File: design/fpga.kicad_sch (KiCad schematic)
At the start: 83 parts, among them J7 DEBUG_FPGA_GPIO, J8 DIGILENT_JTAG_HS2_01X06, SW1 RST, SW2 PROG, U13 XC7S15-FTGB196, U14 IS25LP064A-JKx

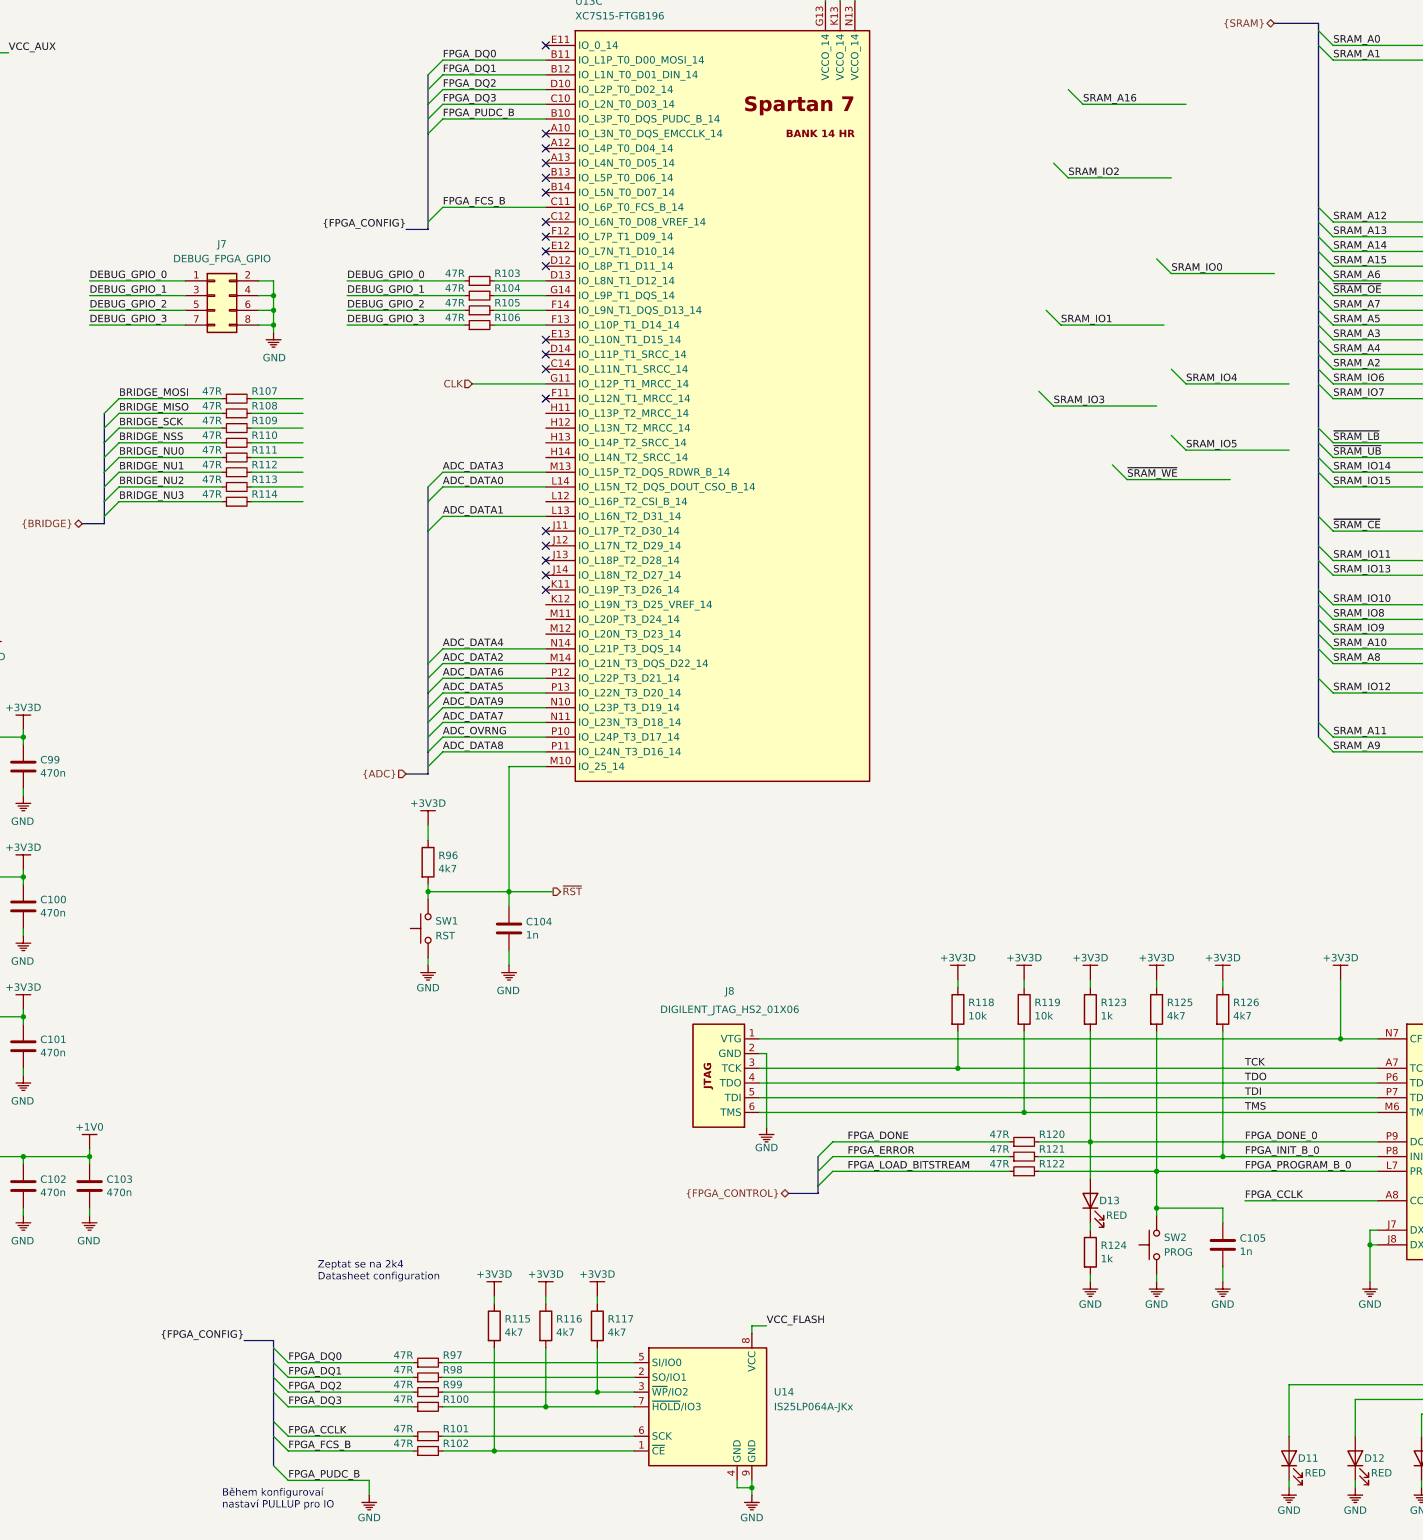
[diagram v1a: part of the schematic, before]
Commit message: Updated ADC layout
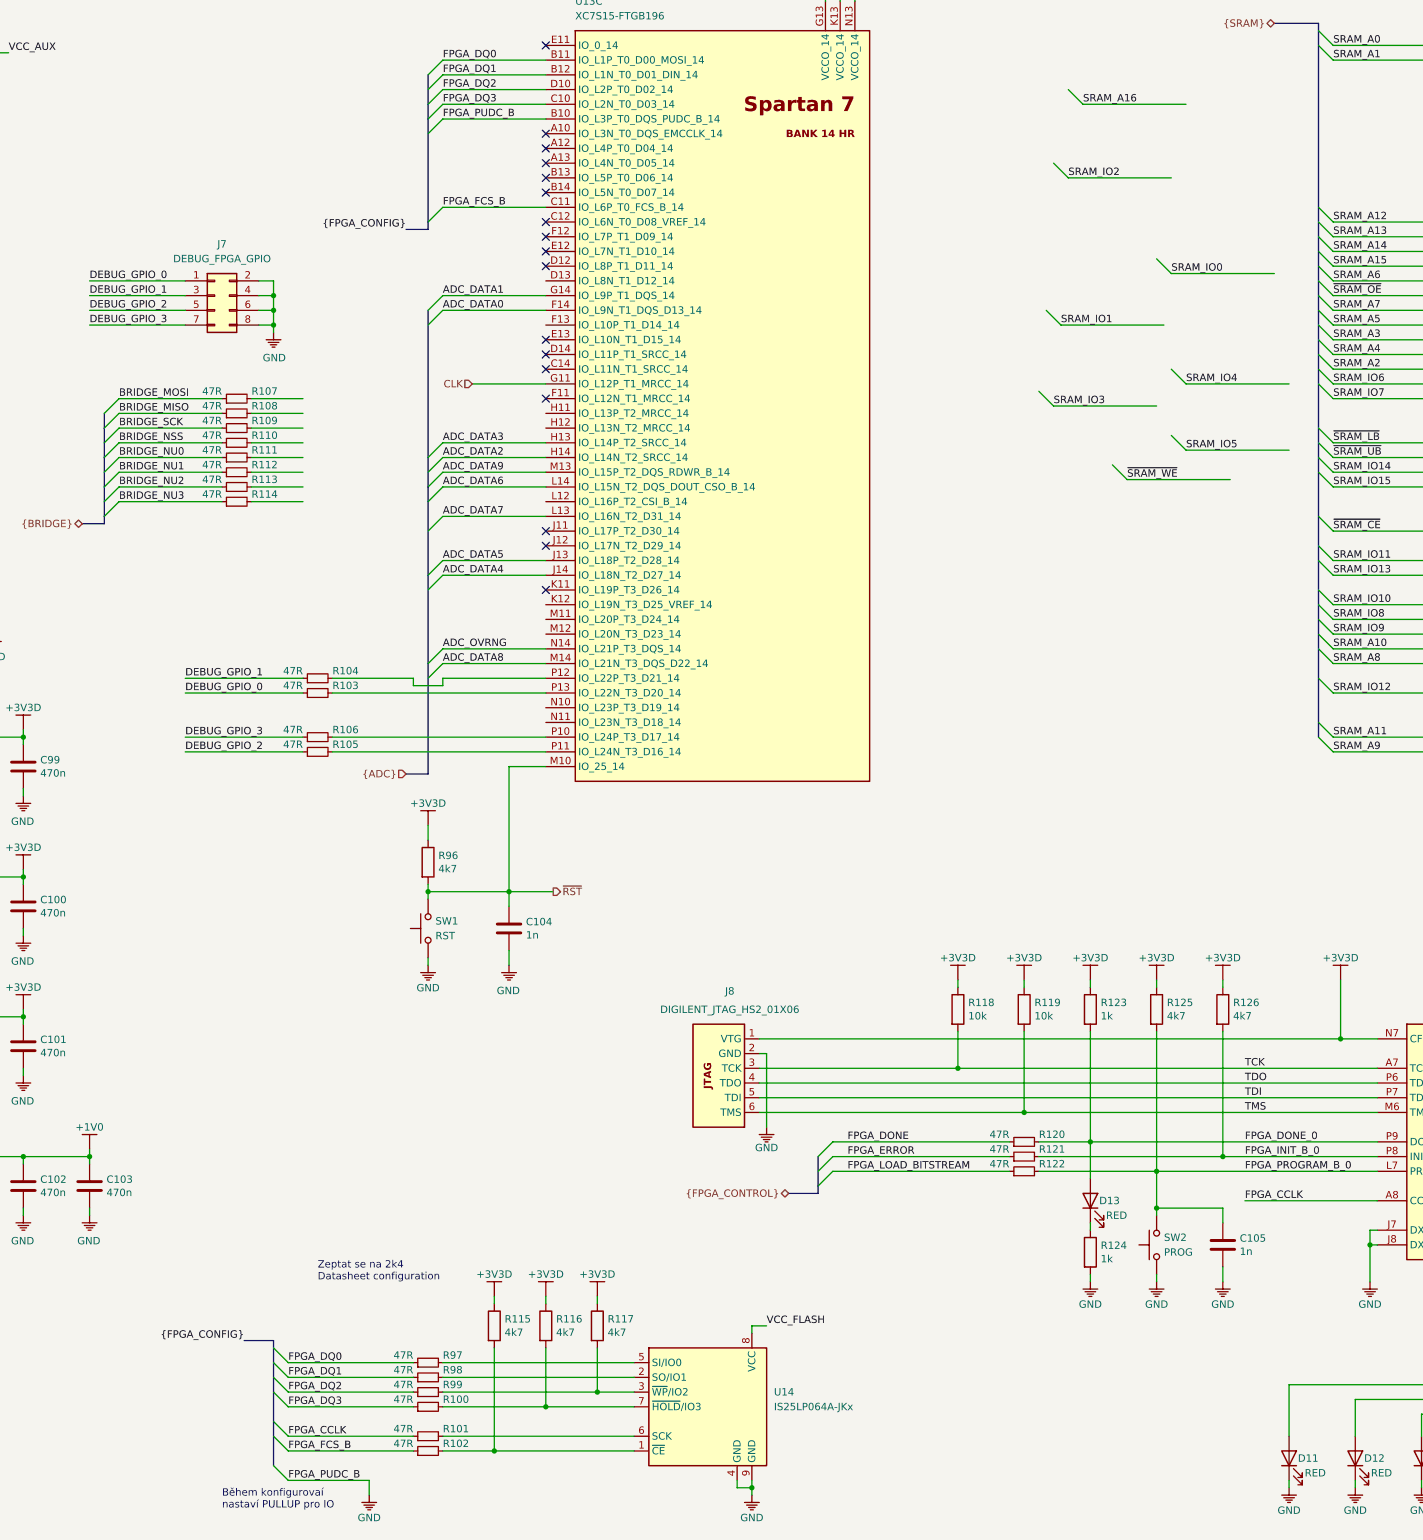
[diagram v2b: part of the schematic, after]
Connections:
- net ADC_DATA0: now also U13.F14 (IO_L9N_T1_DQS_D13_14); no longer U13.L14 (IO_L15N_T2_DQS_DOUT_CSO_B_14)
- net ADC_DATA1: now also U13.G14 (IO_L9P_T1_DQS_14); no longer U13.L13 (IO_L16N_T2_D31_14)
- net ADC_DATA2: now also U13.H14 (IO_L14N_T2_SRCC_14); no longer U13.M14 (IO_L21N_T3_DQS_D22_14)
- net ADC_DATA3: now also U13.H13 (IO_L14P_T2_SRCC_14); no longer U13.M13 (IO_L15P_T2_DQS_RDWR_B_14)
- net ADC_DATA4: now also U13.J14 (IO_L18N_T2_D27_14); no longer U13.N14 (IO_L21P_T3_DQS_14)
- net ADC_DATA5: now also U13.J13 (IO_L18P_T2_D28_14); no longer U13.P13 (IO_L22N_T3_D20_14)
- net ADC_DATA6: now also U13.L14 (IO_L15N_T2_DQS_DOUT_CSO_B_14); no longer U13.P12 (IO_L22P_T3_D21_14)
- net ADC_DATA7: now also U13.L13 (IO_L16N_T2_D31_14); no longer U13.N11 (IO_L23N_T3_D18_14)
- net ADC_DATA8: now also U13.M14 (IO_L21N_T3_DQS_D22_14); no longer U13.P11 (IO_L24N_T3_D16_14)
- net ADC_DATA9: now also U13.M13 (IO_L15P_T2_DQS_RDWR_B_14); no longer U13.N10 (IO_L23P_T3_D19_14)
- net ADC_OVRNG: now also U13.N14 (IO_L21P_T3_DQS_14); no longer U13.P10 (IO_L24P_T3_D17_14)
- net at R105.2: now also U13.P11 (IO_L24N_T3_D16_14); no longer U13.F14 (IO_L9N_T1_DQS_D13_14)
- net at R104.2: now also U13.P12 (IO_L22P_T3_D21_14); no longer U13.G14 (IO_L9P_T1_DQS_14)
- net at R103.2: now also U13.P13 (IO_L22N_T3_D20_14); no longer U13.D13 (IO_L8N_T1_D12_14)
- net at U13.F13 (IO_L10P_T1_D14_14): no longer R106.2
- new net: R106.2, U13.P10 (IO_L24P_T3_D17_14)
- no-connect marks 19 -> 17
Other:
- moved on the sheet: R103, R104, R105, R106

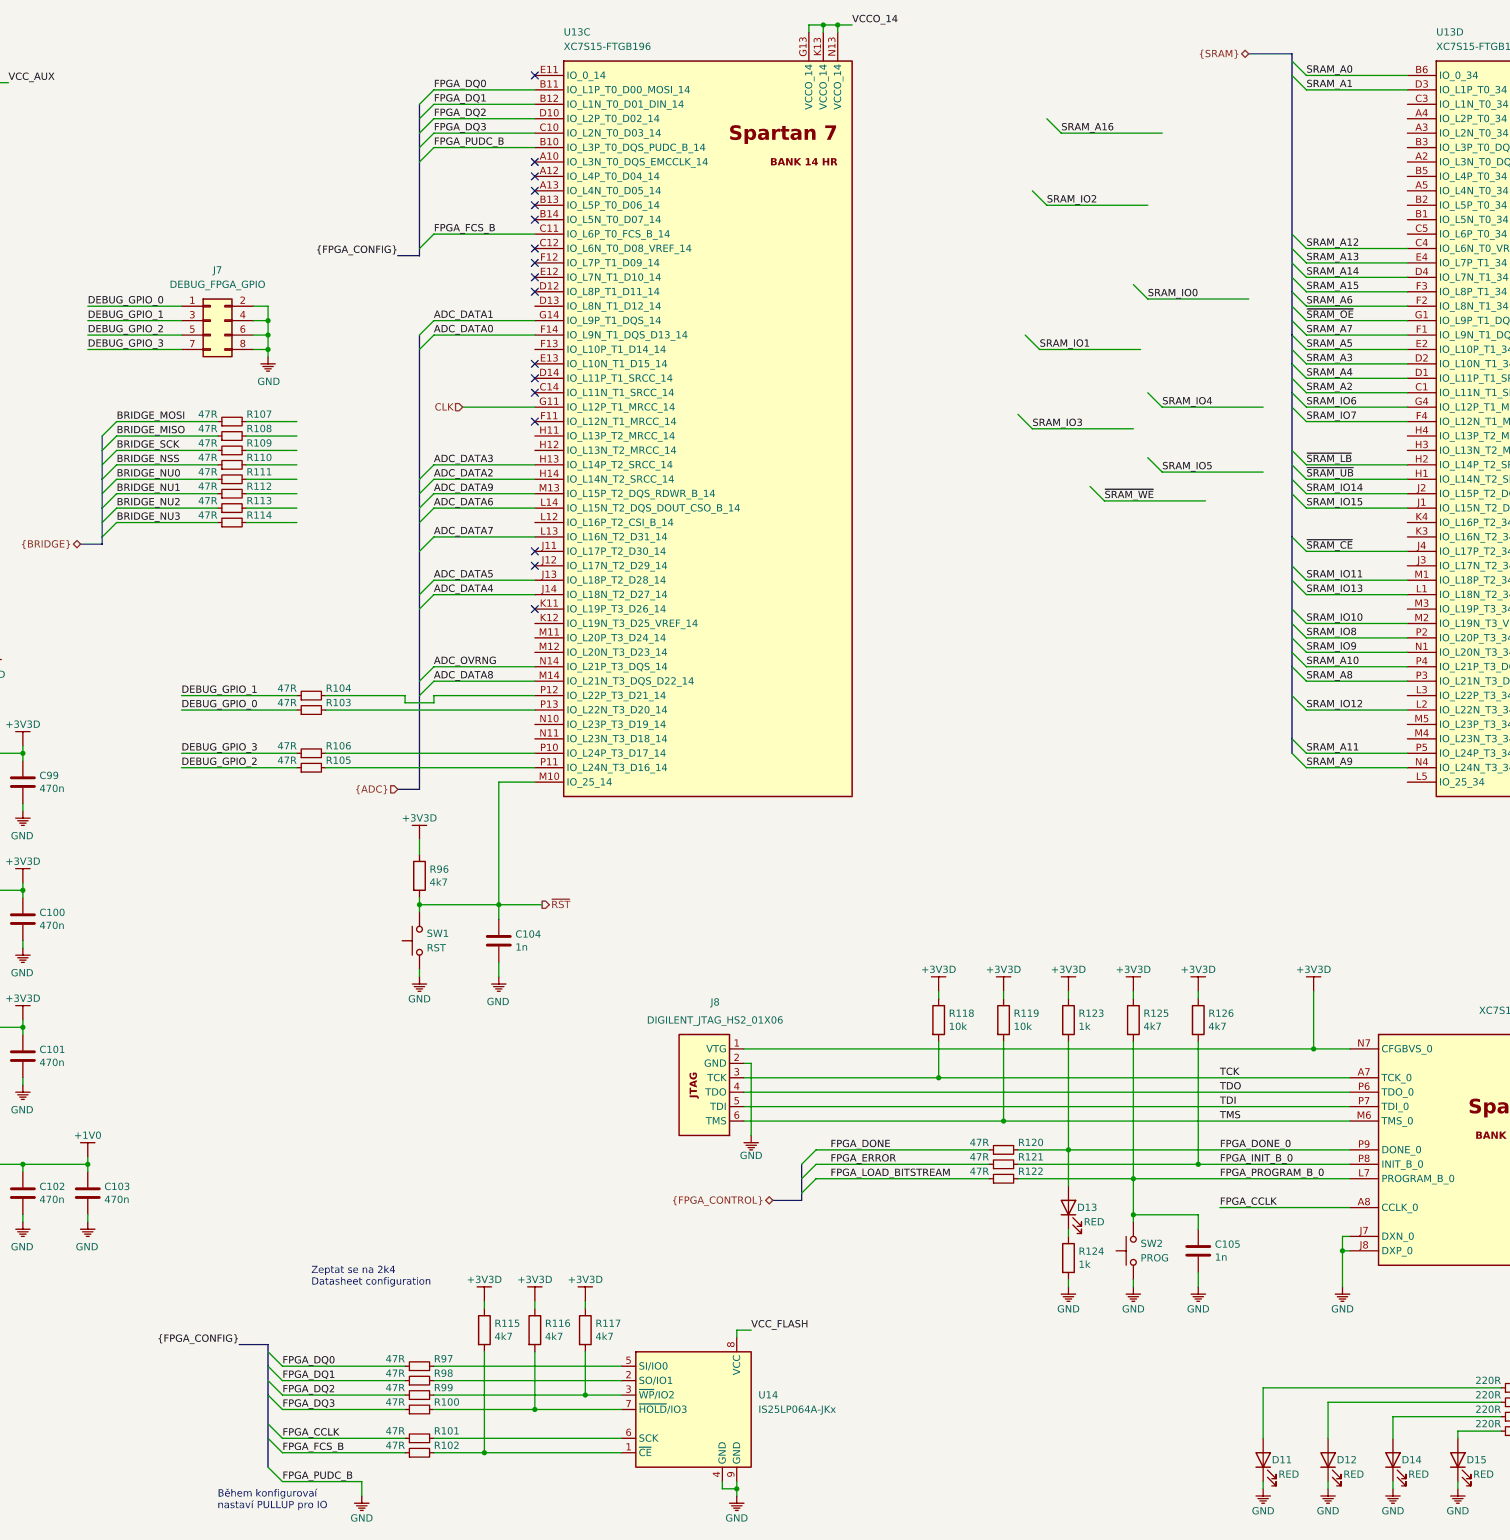
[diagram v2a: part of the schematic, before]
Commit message: Added RAM layout
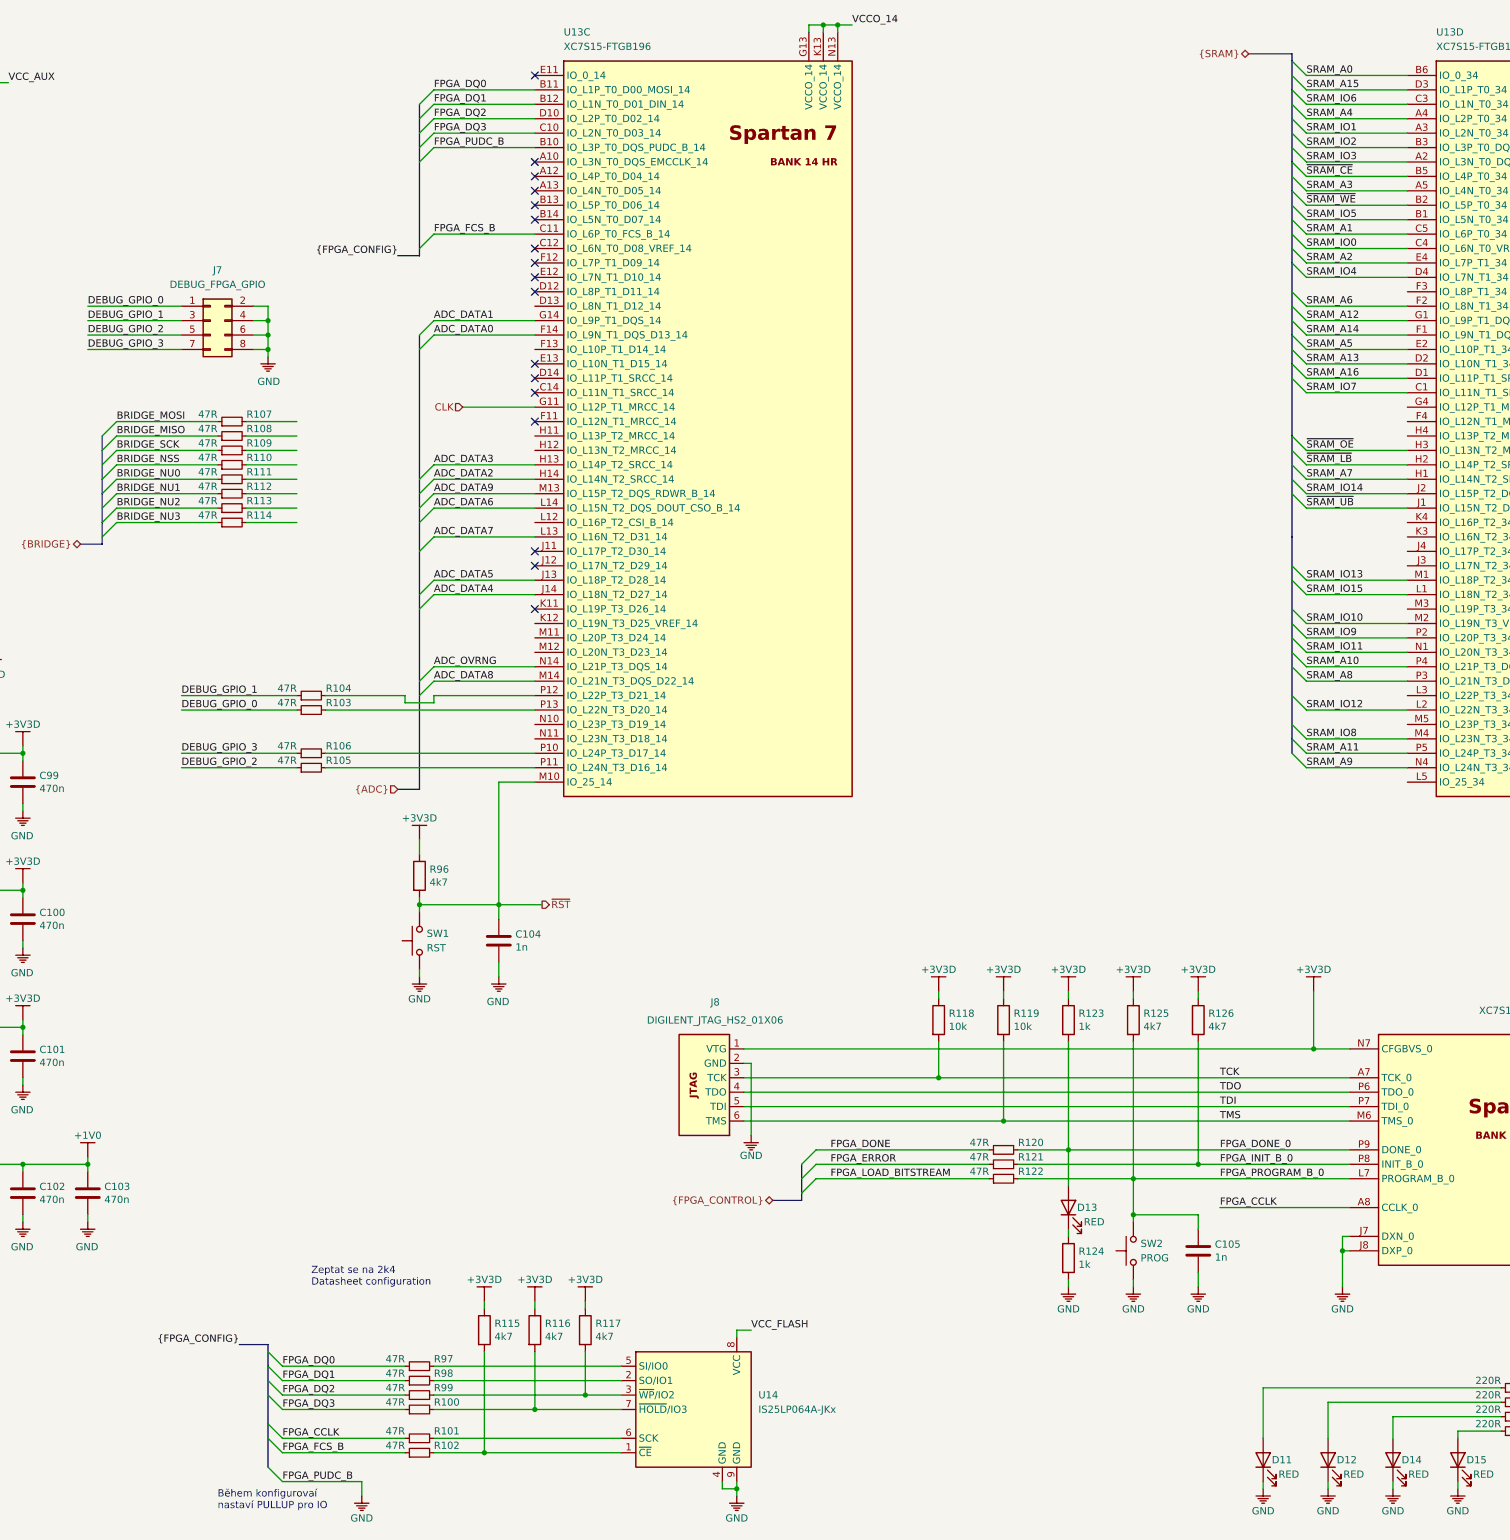
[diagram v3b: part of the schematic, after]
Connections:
- net SRAM_A1: now also U13.C5 (IO_L6P_T0_34); no longer U13.D3 (IO_L1P_T0_34)
- net SRAM_A12: now also U13.G1 (IO_L9P_T1_DQS_34); no longer U13.C4 (IO_L6N_T0_VREF_34)
- net SRAM_A13: now also U13.D2 (IO_L10N_T1_34); no longer U13.E4 (IO_L7P_T1_34)
- net SRAM_A14: now also U13.F1 (IO_L9N_T1_DQS_34); no longer U13.D4 (IO_L7N_T1_34)
- net SRAM_A15: now also U13.D3 (IO_L1P_T0_34); no longer U13.F3 (IO_L8P_T1_34)
- net SRAM_A16: now also U13.D1 (IO_L11P_T1_SRCC_34)
- net SRAM_A2: now also U13.E4 (IO_L7P_T1_34); no longer U13.C1 (IO_L11N_T1_SRCC_34)
- net SRAM_A3: now also U13.A5 (IO_L4N_T0_34); no longer U13.D2 (IO_L10N_T1_34)
- net SRAM_A4: now also U13.A4 (IO_L2P_T0_34); no longer U13.D1 (IO_L11P_T1_SRCC_34)
- net SRAM_A7: now also U13.H1 (IO_L14N_T2_SRCC_34); no longer U13.F1 (IO_L9N_T1_DQS_34)
- net SRAM_IO0: now also U13.C4 (IO_L6N_T0_VREF_34)
- net SRAM_IO1: now also U13.A3 (IO_L2N_T0_34)
- net SRAM_IO11: now also U13.N1 (IO_L20N_T3_34); no longer U13.M1 (IO_L18P_T2_34)
- net SRAM_IO13: now also U13.M1 (IO_L18P_T2_34); no longer U13.L1 (IO_L18N_T2_34)
- net SRAM_IO15: now also U13.L1 (IO_L18N_T2_34); no longer U13.J1 (IO_L15N_T2_DQS_34)
- net SRAM_IO2: now also U13.B3 (IO_L3P_T0_DQS_34)
- net SRAM_IO3: now also U13.A2 (IO_L3N_T0_DQS_34)
- net SRAM_IO4: now also U13.D4 (IO_L7N_T1_34)
- net SRAM_IO5: now also U13.B1 (IO_L5N_T0_34)
- net SRAM_IO6: now also U13.C3 (IO_L1N_T0_34); no longer U13.G4 (IO_L12P_T1_MRCC_34)
- net SRAM_IO7: now also U13.C1 (IO_L11N_T1_SRCC_34); no longer U13.F4 (IO_L12N_T1_MRCC_34)
- net SRAM_IO8: now also U13.M4 (IO_L23N_T3_34); no longer U13.P2 (IO_L20P_T3_34)
- net SRAM_IO9: now also U13.P2 (IO_L20P_T3_34); no longer U13.N1 (IO_L20N_T3_34)
- net ~SRAM_CE: now also U13.B5 (IO_L4P_T0_34); no longer U13.J4 (IO_L17P_T2_34)
- net ~SRAM_OE: now also U13.H3 (IO_L13N_T2_MRCC_34); no longer U13.G1 (IO_L9P_T1_DQS_34)
- net ~SRAM_UB: now also U13.J1 (IO_L15N_T2_DQS_34); no longer U13.H1 (IO_L14N_T2_SRCC_34)
- net ~SRAM_WE: now also U13.B2 (IO_L5P_T0_34)
